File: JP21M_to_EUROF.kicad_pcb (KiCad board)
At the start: 2 copper layers, 58.4 x 24.8 mm, 2 parts, among them J1 SCART-F, J2 SCART-F

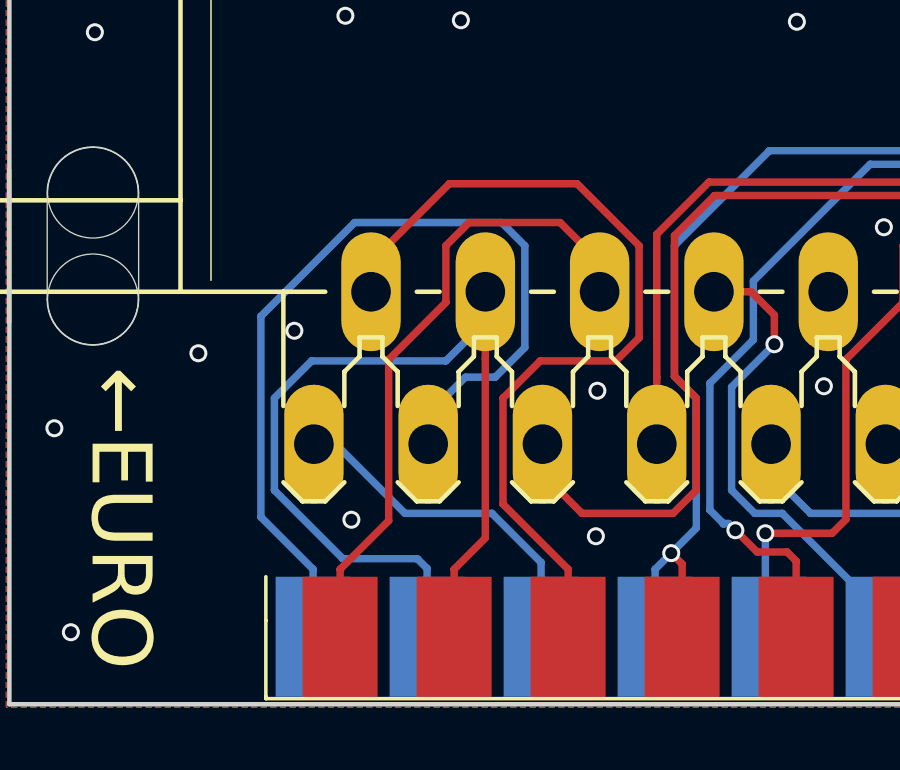
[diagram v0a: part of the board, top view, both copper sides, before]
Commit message: fixed incorrect audio pins for JP21
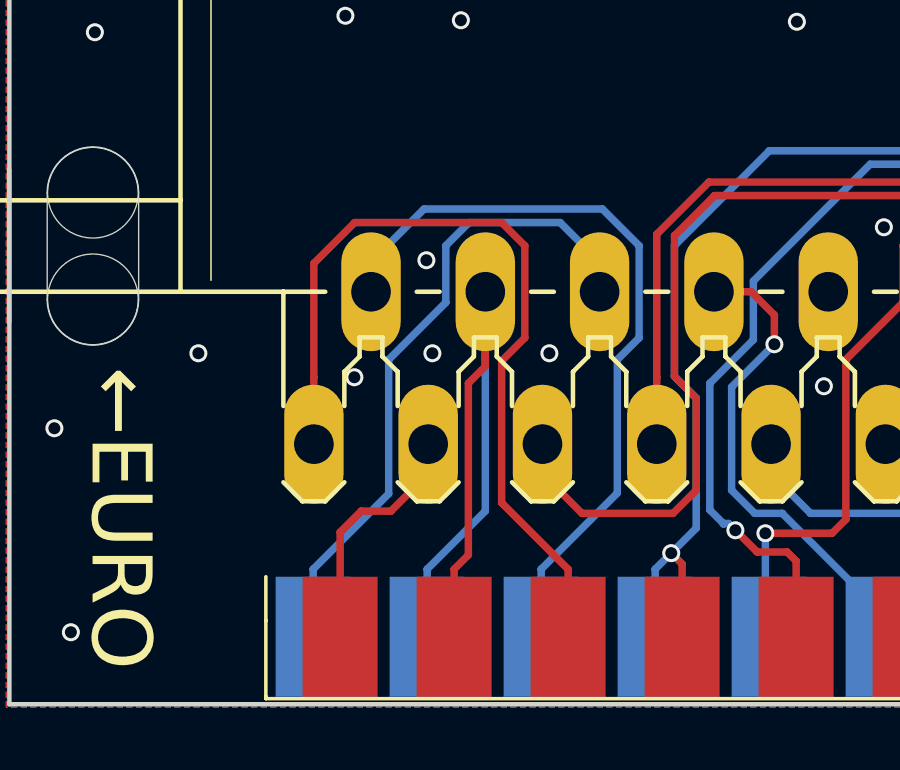
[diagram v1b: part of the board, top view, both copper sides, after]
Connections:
- J2 pad 1: L_OUT -> L_IN
- J2 pad 2: L_IN -> L_OUT
- J2 pad 5: RT_OUT -> RT_IN
- J2 pad 6: RT_IN -> RT_OUT
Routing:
- net L_OUT: track 30.3 -> 8.22 mm
- net RT_OUT: track 11.7 -> 29.0 mm
- net A_GND: track 32.5 -> 24.2 mm
- net RT_IN: track 29.2 -> 25.6 mm
